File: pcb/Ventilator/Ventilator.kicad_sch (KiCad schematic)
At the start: 69 parts, among them J1 Screw_Terminal_01x08, J2 Screw_Terminal_01x02, J3 Screw_Terminal_01x08, K1 FINDER-40.52.7.012.0000, K2 FINDER-40.52.7.012.0000, K3 FINDER-40.52.7.012.0000, Q1 NUD3160, Q2 NUD3160, Q3 NUD3160, SW1 Reset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

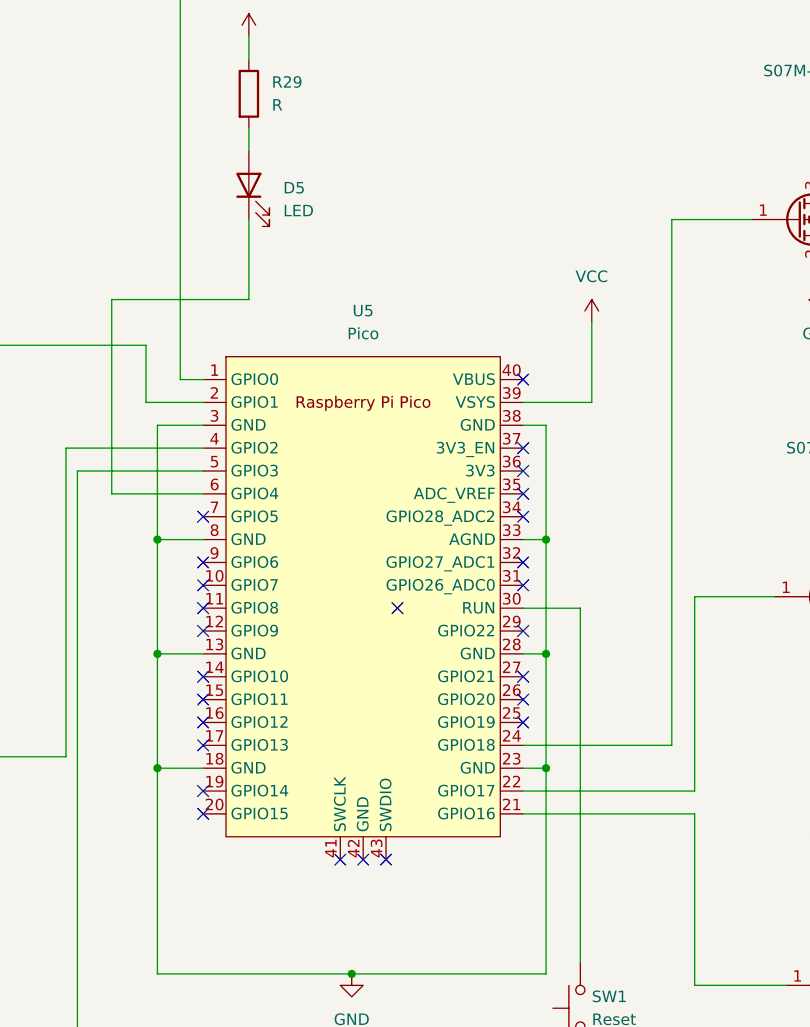
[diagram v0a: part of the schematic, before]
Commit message: -components placed
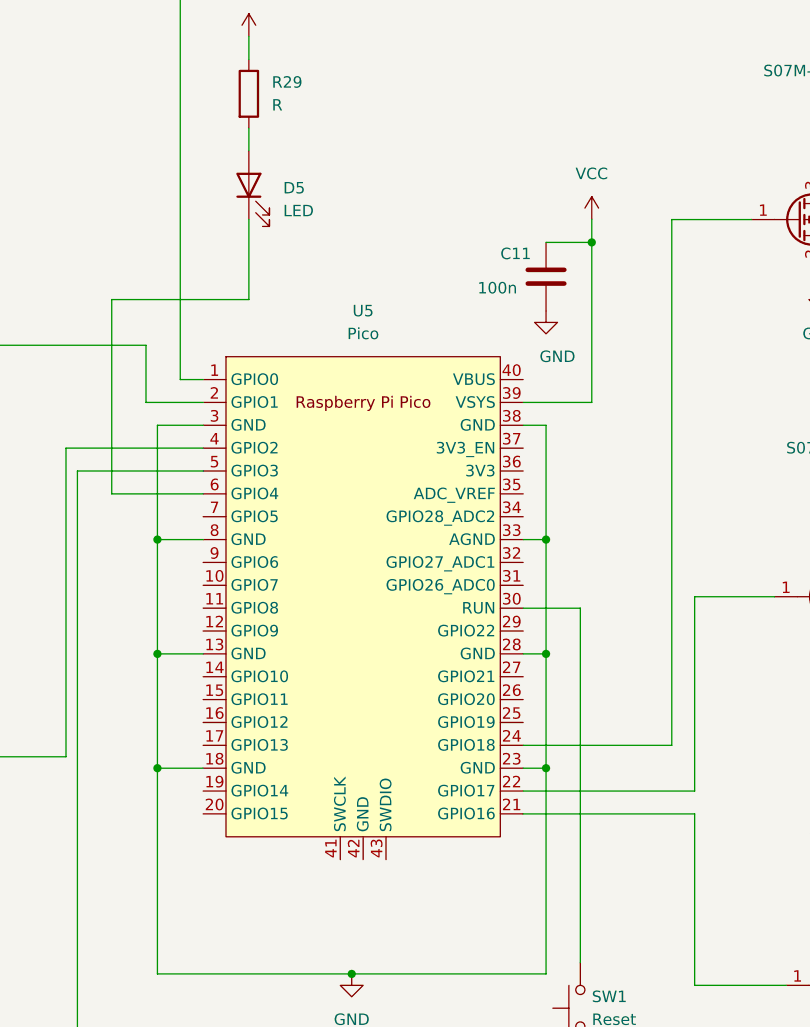
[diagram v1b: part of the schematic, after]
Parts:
- added C11: 100n, Capacitor_SMD:C_1206_3216Metric_Pad1.33x1.80mm_HandSolder, symbol Device:C
- U5: footprint RPi_Pico:RPi_Pico_SMD_TH -> MCU_RaspberryPi_and_Boards:RPi_Pico_SMD_TH
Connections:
- net GND: now also C11.2
- net VCC: now also C11.1
- no-connect marks 46 -> 20

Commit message: - as send to JCLPCB
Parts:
- added TP1, TP2, TP3, TP4: TestPoint, TestPoint:TestPoint_Bridge_Pitch2.54mm_Drill1.0mm, symbol Connector:TestPoint
- R28: value R -> 10k
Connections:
- net at U5.5 (GPIO3): no longer R28.2
- net at Q3.1 (G): now also U5.34 (GPIO28_ADC2); no longer U5.21 (GPIO16)
- net IN3: now reaches R27.2, U5.4 (GPIO2)
- net IN3: now also TP3.1
- net at U5.1 (GPIO0): now also D5.1 (K); no longer R25.2
- net IN2: now reaches U5.19 (GPIO14)
- net IN2: now also R26.2, TP2.1
- net IN4: now reaches U5.2 (GPIO1)
- net IN4: now also R28.2, TP4.1; no longer R26.2
- net IN1: now reaches U5.20 (GPIO15)
- net IN1: now also R25.2, TP1.1
- net at U5.22 (GPIO17): no longer Q2.1 (G)
- net at U5.29 (GPIO22): now also Q2.1 (G)
- net at U5.6 (GPIO4): no longer D5.1 (K)
- no-connect marks 20 -> 45

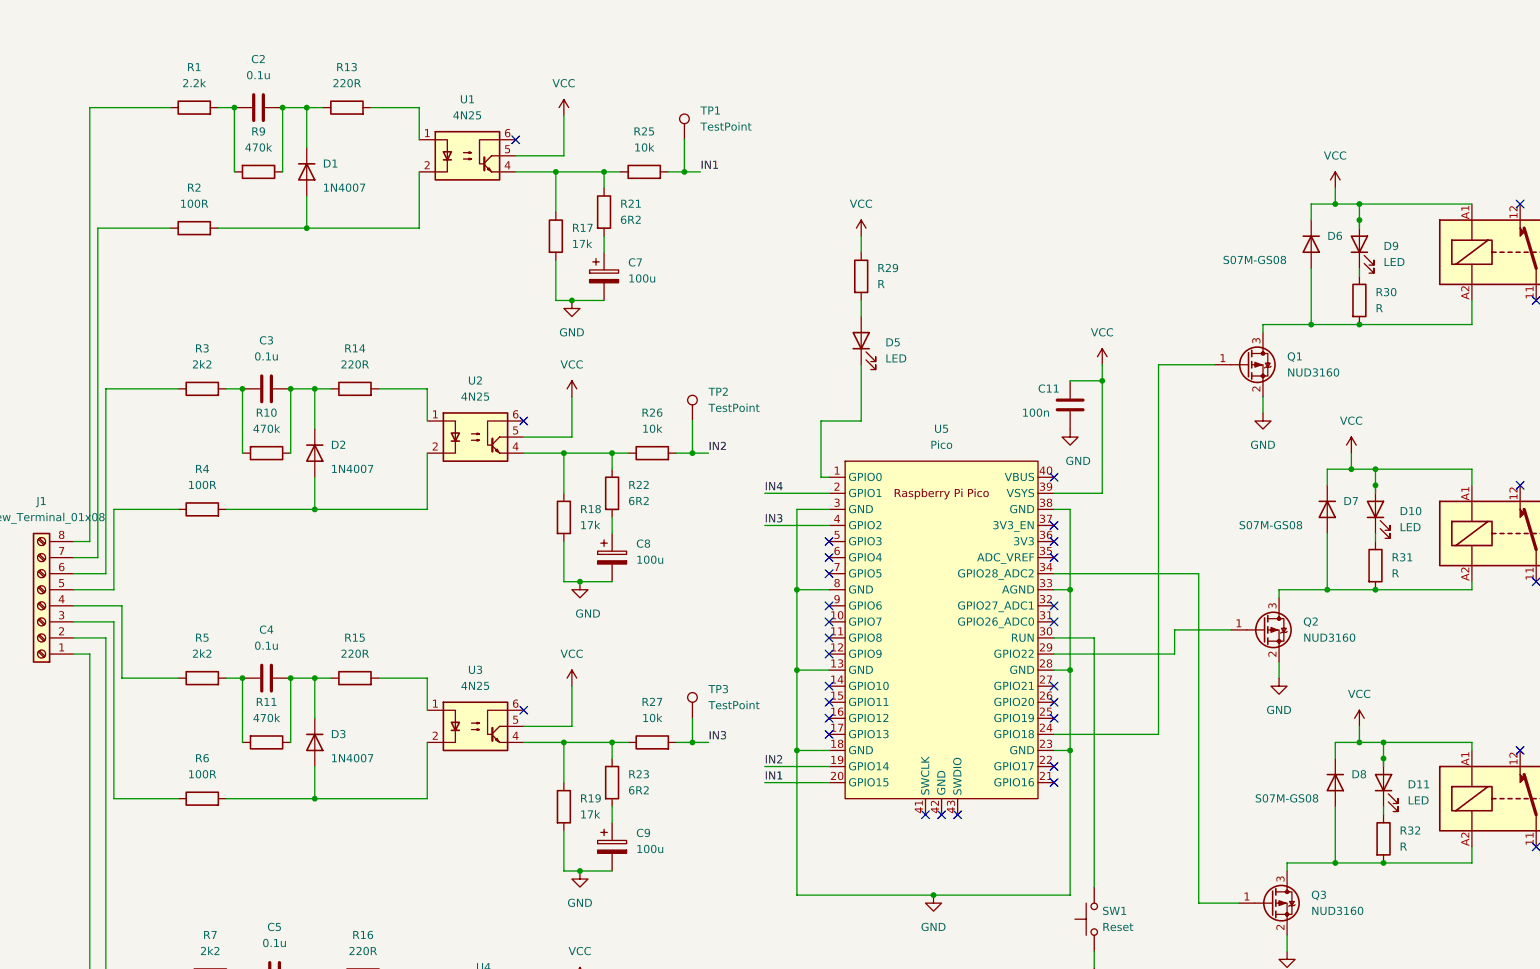
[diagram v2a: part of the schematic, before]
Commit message: - resister values
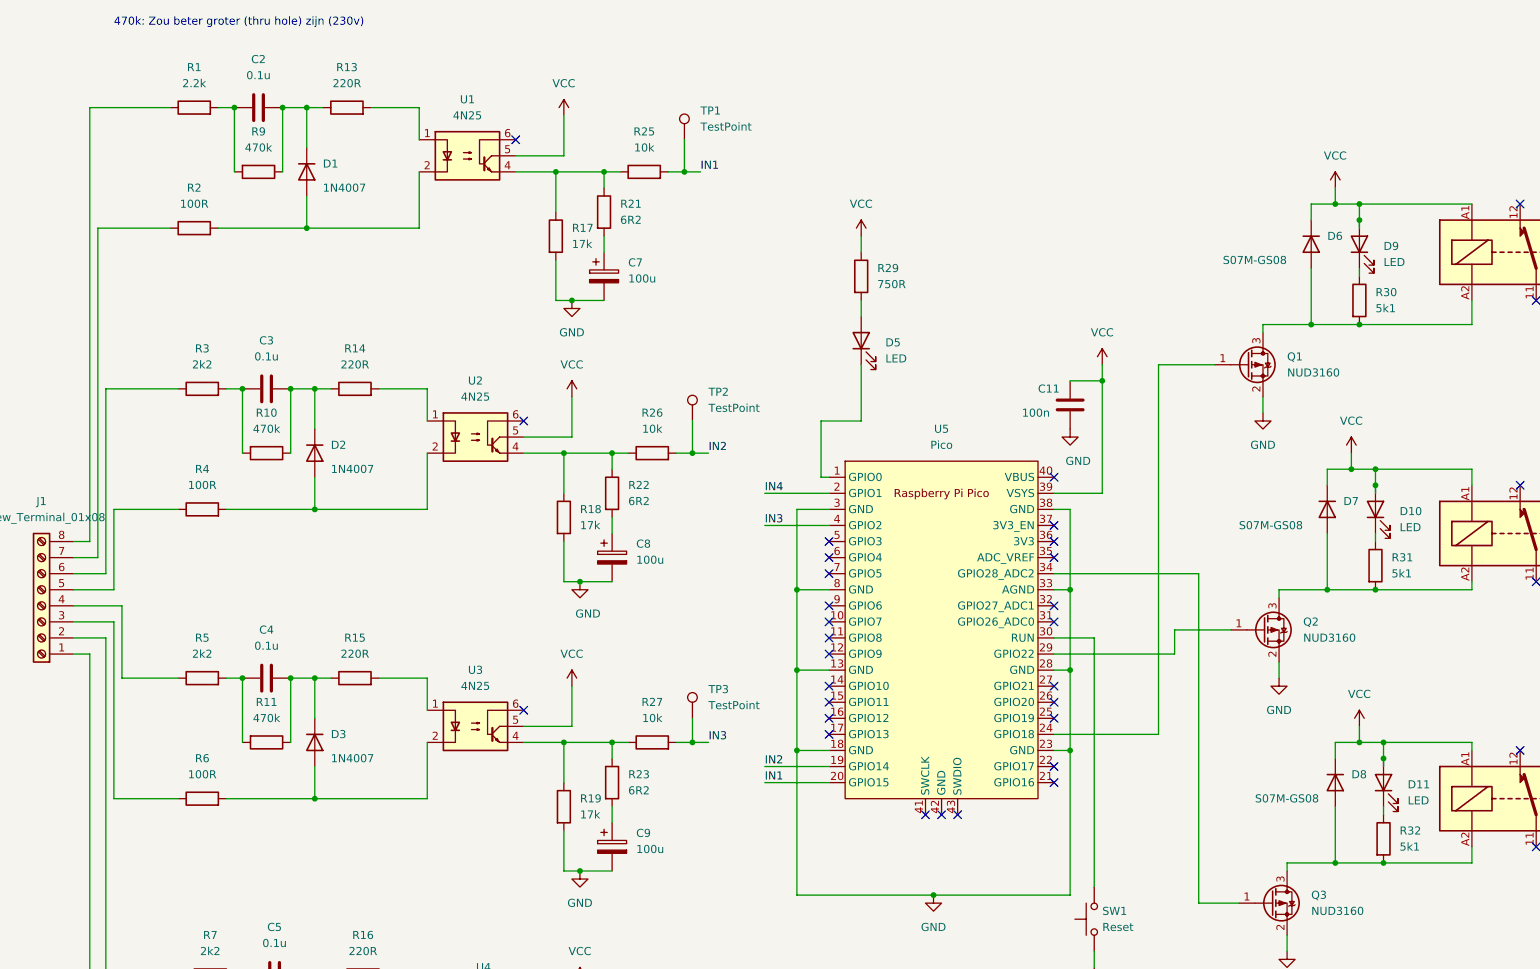
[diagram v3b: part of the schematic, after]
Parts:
- R29: value R -> 750R
- R30, R31, R32: value R -> 5k1
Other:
- note added: "470k: Zou beter groter (thru hole) zijn (230v)"
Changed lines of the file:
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@@
+    (effects (font (size 1.27 1.27)) (justify left bottom))
+  )
+  (text "470k: Zou beter groter (thru hole) zijn (230v)" (at 27.94 39.37 0)
     (effects (font (size 1.27 1.27)) (justify left bottom))
   )
@@
       (effects (font (size 1.27 1.27)) (justify left))
     )
-    (property "Value" "R" (id 1) (at 229.87 125.7299 0)
+    (property "Value" "5k1" (id 1) (at 229.87 125.7299 0)
       (effects (font (size 1.27 1.27)) (justify left))
     )
@@
       (effects (font (size 1.27 1.27)) (justify left))
     )
-    (property "Value" "R" (id 1) (at 227.33 83.8199 0)
+    (property "Value" "5k1" (id 1) (at 227.33 83.8199 0)
       (effects (font (size 1.27 1.27)) (justify left))
     )
@@
       (effects (font (size 1.27 1.27)) (justify left))
     )
-    (property "Value" "R" (id 1) (at 148.59 80.0099 0)
+    (property "Value" "750R" (id 1) (at 148.59 80.0099 0)
       (effects (font (size 1.27 1.27)) (justify left))
     )
@@
       (effects (font (size 1.27 1.27)) (justify left))
     )
-    (property "Value" "R" (id 1) (at 231.14 168.9099 0)
+    (property "Value" "5k1" (id 1) (at 231.14 168.9099 0)
       (effects (font (size 1.27 1.27)) (justify left))
     )
@@
     )
     (path "/82857fc6-03bc-46a9-a64b-27e770203968"
-      (reference "R29") (unit 1) (value "R") (footprint "Resistor_SMD:R_0805_2012Metric_Pad1.20x1.40mm_HandSolder")
+      (reference "R29") (unit 1) (value "750R") (footprint "Resistor_SMD:R_0805_2012Metric_Pad1.20x1.40mm_HandSolder")
     )
     (path "/41668391-5281-4cf3-a2f8-cb6a930df4d8"
-      (reference "R30") (unit 1) (value "R") (footprint "Resistor_SMD:R_0805_2012Metric_Pad1.20x1.40mm_HandSolder")
+      (reference "R30") (unit 1) (value "5k1") (footprint "Resistor_SMD:R_0805_2012Metric_Pad1.20x1.40mm_HandSolder")
     )
     (path "/12359d3c-84a9-46ab-bae0-ef123a135809"
-      (reference "R31") (unit 1) (value "R") (footprint "Resistor_SMD:R_0805_2012Metric_Pad1.20x1.40mm_HandSolder")
+      (reference "R31") (unit 1) (value "5k1") (footprint "Resistor_SMD:R_0805_2012Metric_Pad1.20x1.40mm_HandSolder")
     )
     (path "/bc8747e1-cabf-45f1-9568-bf42b6284d0a"
-      (reference "R32") (unit 1) (value "R") (footprint "Resistor_SMD:R_0805_2012Metric_Pad1.20x1.40mm_HandSolder")
+      (reference "R32") (unit 1) (value "5k1") (footprint "Resistor_SMD:R_0805_2012Metric_Pad1.20x1.40mm_HandSolder")
     )
     (path "/f8587f72-2870-4176-82cb-531be667074a"

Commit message: - added rp2040, multiple sheets, etc...
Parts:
- removed C1: 10u, Capacitor_SMD:C_0805_2012Metric_Pad1.18x1.45mm_HandSolder, symbol Device:C
- removed C10, C7, C8, C9: 100u, Capacitor_SMD:C_1206_3216Metric_Pad1.33x1.80mm_HandSolder, symbol Device:C_Polarized
- removed C11: 100n, Capacitor_SMD:C_1206_3216Metric_Pad1.33x1.80mm_HandSolder, symbol Device:C
- removed C2, C3, C4, C5: 0.1u, Capacitor_THT:C_Rect_L18.0mm_W5.0mm_P15.00mm_FKS3_FKP3, symbol Device:C
- removed C6: 22u, Capacitor_SMD:C_0805_2012Metric_Pad1.18x1.45mm_HandSolder, symbol Device:C
- removed D1, D2, D3, D4: 1N4007, Diode_THT:D_DO-41_SOD81_P10.16mm_Horizontal, symbol Diode:1N4007
- removed D10, D11, D5, D9: LED, LED_THT:LED_D3.0mm, symbol Device:LED
- removed D6, D7, D8: S07M-GS08, Diode_SMD:D_SMF, symbol Device:D
- removed J1, J3: Screw_Terminal_01x08, TerminalBlock_Phoenix:TerminalBlock_Phoenix_MKDS-1,5-8_1x08_P5.00mm_Horizontal, symbol Connector:Screw_Terminal_01x08
- removed J2: Screw_Terminal_01x02, TerminalBlock:TerminalBlock_bornier-2_P5.08mm, symbol Connector:Screw_Terminal_01x02
- removed K1, K2, K3: FINDER-40.52.7.012.0000, Relay_THT:Relay_DPDT_Finder_40.52, symbol Relay:FINDER-40.52
- removed PS1: R-78AA3.3-0.5SMD-R, R-78AA3.3-1:CONV_R-78AA3.3-1.0SMD, symbol Power:R-78AA3.3-1.0SMD
- removed Q1, Q2, Q3: NUD3160, Package_TO_SOT_SMD:SOT-23, symbol Transistor_FET:TSM2301ACX
- removed R1: 2.2k, Resistor_THT:R_Axial_DIN0414_L11.9mm_D4.5mm_P15.24mm_Horizontal, symbol Device:R
- removed R10, R11, R12, R9: 470k, Resistor_SMD:R_0805_2012Metric_Pad1.20x1.40mm_HandSolder, symbol Device:R
- removed R13, R14, R15, R16: 220R, Resistor_SMD:R_0805_2012Metric_Pad1.20x1.40mm_HandSolder, symbol Device:R
- removed R17, R18, R19, R20: 17k, Resistor_SMD:R_0805_2012Metric_Pad1.20x1.40mm_HandSolder, symbol Device:R
- removed R2, R4, R6, R8: 100R, Resistor_SMD:R_0805_2012Metric_Pad1.20x1.40mm_HandSolder, symbol Device:R
- removed R21, R22, R23, R24: 6R2, Resistor_SMD:R_0805_2012Metric_Pad1.20x1.40mm_HandSolder, symbol Device:R
- removed R25, R26, R27, R28: 10k, Resistor_SMD:R_0805_2012Metric_Pad1.20x1.40mm_HandSolder, symbol Device:R
- removed R29: 750R, Resistor_SMD:R_0805_2012Metric_Pad1.20x1.40mm_HandSolder, symbol Device:R
- removed R3, R5, R7: 2k2, Resistor_THT:R_Axial_DIN0414_L11.9mm_D4.5mm_P15.24mm_Horizontal, symbol Device:R
- removed R30, R31, R32: 5k1, Resistor_SMD:R_0805_2012Metric_Pad1.20x1.40mm_HandSolder, symbol Device:R
- removed SW1: Reset, Button_Switch_SMD:SW_SPST_EVPBF, symbol Switch:SW_Push
- removed TP1, TP2, TP3, TP4: TestPoint, TestPoint:TestPoint_Bridge_Pitch2.54mm_Drill1.0mm, symbol Connector:TestPoint
- removed U1, U2, U3, U4: 4N25, Package_DIP:DIP-6_W7.62mm, symbol Isolator:4N25
- removed U5: Pico, MCU_RaspberryPi_and_Boards:RPi_Pico_SMD_TH, symbol MCU_RaspberryPi_and_Boards:Pico
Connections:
- no-connect marks 45 -> 0
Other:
- added sheet CPU (cpu.kicad_sch)
- added sheet Input (Input.kicad_sch)
- added sheet Output (Output.kicad_sch)
- added sheet Power (Power.kicad_sch)
- note removed: "470k: Zou beter groter (thru hole) zijn (230v)"
- note removed: "Power Supply 12VDC-DIN RAIL 78.12.1.230.1200"
